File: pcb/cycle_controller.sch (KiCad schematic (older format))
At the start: 51 parts

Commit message: BOM, fixes
Finished assigning parts, footprints except generic resistors
Added series resistors for logic signals received by UI computer to protect against UI computer power-down
Added tolerance notes on main schem
Replaced PSol fuse with PTC
Enlarged PSol driver bypass resistors to 0 ohm
Changed PSol unpopulated current-limiting resistor to divider
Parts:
- C? (x9): Dielectric (none) -> X7R; Manufacturer (none) -> Kemet; Manufacturer PN (none) -> C0603C104K5RACTU; Voltage (none) -> 50V
- C? (x3): Dielectric (none) -> X7R; Manufacturer (none) -> Kemet; Manufacturer PN (none) -> C0805C105K5RACTU; Voltage (none) -> 50V
- C? (x2): Manufacturer (none) -> Kemet; Manufacturer PN (none) -> C0603C180J5GACTU; Voltage (none) -> 50V
- C? (x2): Dielectric (none) -> NP0; Manufacturer (none) -> Kemet; Manufacturer PN (none) -> C0603C689J5GACTU; Voltage (none) -> 50V
- J?: Manufacturer (none) -> Sullins; Manufacturer PN (none) -> PPPC061LFBN-RC
- J? (x2): Manufacturer (none) -> Sullins; Manufacturer PN (none) -> PPPC081LFBN-RC
- J?: Manufacturer (none) -> Sullins; Manufacturer PN (none) -> PPPC101LFBN-RC
- J?: Manufacturer (none) -> Molex; Manufacturer PN (none) -> 503182-1852
- J? (x2): Manufacturer (none) -> Molex; Manufacturer PN (none) -> 43650-0315
- SW? (x2): footprint RespiraWorks_Std:SW_Push_6x6_TD-0341 -> RespiraWorks_Std:SW_Push_6x6; Manufacturer (none) -> C&K; Manufacturer PN (none) -> PTS645SK50SMTR92 LFS
- U?: Manufacturer (none) -> STMicroelectronics; Manufacturer PN (none) -> STM32L496VGT6; Sourcing Notes (none) -> Either ...VGT6 or ...VGT3 can be used
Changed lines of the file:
@@
 F 2 "RespiraWorks_Std:C_0603_1608Metric" H 7538 850 50  0001 C CNN
 F 3 "~" H 7500 1000 50  0001 C CNN
+F 4 "X7R" H 7500 1000 50  0001 C CNN "Dielectric"
+F 5 "Kemet" H 7500 1000 50  0001 C CNN "Manufacturer"
+F 6 "C0603C104K5RACTU" H 7500 1000 50  0001 C CNN "Manufacturer PN"
+F 7 "50V" H 7500 1000 50  0001 C CNN "Voltage"
 	1    7500 1000
 	1    0    0    -1
@@
 F 2 "RespiraWorks_Std:C_0603_1608Metric" H 7838 850 50  0001 C CNN
 F 3 "~" H 7800 1000 50  0001 C CNN
+F 4 "X7R" H 7800 1000 50  0001 C CNN "Dielectric"
+F 5 "Kemet" H 7800 1000 50  0001 C CNN "Manufacturer"
+F 6 "C0603C104K5RACTU" H 7800 1000 50  0001 C CNN "Manufacturer PN"
+F 7 "50V" H 7800 1000 50  0001 C CNN "Voltage"
 	1    7800 1000
 	1    0    0    -1
@@
 F 2 "RespiraWorks_Std:C_0603_1608Metric" H 8188 850 50  0001 C CNN
 F 3 "~" H 8150 1000 50  0001 C CNN
+F 4 "X7R" H 8150 1000 50  0001 C CNN "Dielectric"
+F 5 "Kemet" H 8150 1000 50  0001 C CNN "Manufacturer"
+F 6 "C0603C104K5RACTU" H 8150 1000 50  0001 C CNN "Manufacturer PN"
+F 7 "50V" H 8150 1000 50  0001 C CNN "Voltage"
 	1    8150 1000
 	1    0    0    -1
@@
 F 2 "RespiraWorks_Std:C_0603_1608Metric" H 8488 850 50  0001 C CNN
 F 3 "~" H 8450 1000 50  0001 C CNN
+F 4 "X7R" H 8450 1000 50  0001 C CNN "Dielectric"
+F 5 "Kemet" H 8450 1000 50  0001 C CNN "Manufacturer"
+F 6 "C0603C104K5RACTU" H 8450 1000 50  0001 C CNN "Manufacturer PN"
+F 7 "50V" H 8450 1000 50  0001 C CNN "Voltage"
 	1    8450 1000
 	1    0    0    -1
@@
 F 2 "RespiraWorks_Std:C_0603_1608Metric" H 9588 900 50  0001 C CNN
 F 3 "~" H 9550 1050 50  0001 C CNN
+F 4 "X7R" H 9550 1050 50  0001 C CNN "Dielectric"
+F 5 "Kemet" H 9550 1050 50  0001 C CNN "Manufacturer"
+F 6 "C0603C104K5RACTU" H 9550 1050 50  0001 C CNN "Manufacturer PN"
+F 7 "50V" H 9550 1050 50  0001 C CNN "Voltage"
 	1    9550 1050
 	1    0    0    -1
@@
 F 2 "RespiraWorks_Std:C_0603_1608Metric" H 9938 900 50  0001 C CNN
 F 3 "~" H 9900 1050 50  0001 C CNN
+F 4 "X7R" H 9900 1050 50  0001 C CNN "Dielectric"
+F 5 "Kemet" H 9900 1050 50  0001 C CNN "Manufacturer"
+F 6 "C0805C105K5RACTU" H 9900 1050 50  0001 C CNN "Manufacturer PN"
+F 7 "50V" H 9900 1050 50  0001 C CNN "Voltage"
 	1    9900 1050
 	1    0    0    -1
@@
 F 2 "RespiraWorks_Std:C_0603_1608Metric" H 4738 1600 50  0001 C CNN
 F 3 "~" H 4700 1750 50  0001 C CNN
+F 4 "X7R" H 4700 1750 50  0001 C CNN "Dielectric"
+F 5 "Kemet" H 4700 1750 50  0001 C CNN "Manufacturer"
+F 6 "C0603C104K5RACTU" H 4700 1750 50  0001 C CNN "Manufacturer PN"
+F 7 "50V" H 4700 1750 50  0001 C CNN "Voltage"
 	1    4700 1750
 	1    0    0    -1
@@
 F 0 "SW?" V 4054 1948 50  0000 L CNN
 F 1 "Reset CC" V 4145 1948 50  0000 L CNN
-F 2 "RespiraWorks_Std:SW_Push_6x6_TD-0341" H 4100 2000 50  0001 C CNN
+F 2 "RespiraWorks_Std:SW_Push_6x6" H 4100 2000 50  0001 C CNN
 F 3 "" H 4100 2000 50  0001 C CNN
+F 4 "C&K" H 4100 1800 50  0001 C CNN "Manufacturer"
+F 5 "PTS645SK50SMTR92 LFS" H 4100 1800 50  0001 C CNN "Manufacturer PN"
 	1    4100 1800
 	0    1    1    0
@@
 F 4 "DNP" V 2600 2500 50  0000 L CNN "DNP"
 F 5 "NP0" H 2550 2700 50  0001 C CNN "Dielectric"
+F 6 "Kemet" H 2550 2700 50  0001 C CNN "Manufacturer"
+F 7 "C0603C180J5GACTU" H 2550 2700 50  0001 C CNN "Manufacturer PN"
+F 8 "50V" H 2550 2700 50  0001 C CNN "Voltage"
 	1    2550 2700
 	0    -1   -1   0
@@
 F 4 "DNP" V 2600 3050 50  0000 L CNN "DNP"
 F 5 "NP0" H 2550 3250 50  0001 C CNN "Dielectric"
+F 6 "Kemet" H 2550 3250 50  0001 C CNN "Manufacturer"
+F 7 "C0603C180J5GACTU" H 2550 3250 50  0001 C CNN "Manufacturer PN"
+F 8 "50V" H 2550 3250 50  0001 C CNN "Voltage"
 	1    2550 3250
 	0    -1   -1   0
@@
 F 3 "~" H 3600 5050 50  0001 C CNN
 F 4 "" V 3950 5050 50  0001 C CNN "DNP"
+F 5 "NP0" H 3600 5050 50  0001 C CNN "Dielectric"
+F 6 "Kemet" H 3600 5050 50  0001 C CNN "Manufacturer"
+F 7 "C0603C689J5GACTU" H 3600 5050 50  0001 C CNN "Manufacturer PN"
+F 8 "50V" H 3600 5050 50  0001 C CNN "Voltage"
 	1    3600 5050
 	0    1    1    0
@@
 F 0 "SW?" V 2154 4698 50  0000 L CNN
 F 1 "User TBD" V 2245 4698 50  0000 L CNN
-F 2 "RespiraWorks_Std:SW_Push_6x6_TD-0341" H 2200 4750 50  0001 C CNN
+F 2 "RespiraWorks_Std:SW_Push_6x6" H 2200 4750 50  0001 C CNN
 F 3 "" H 2200 4750 50  0001 C CNN
+F 4 "C&K" H 2200 4550 50  0001 C CNN "Manufacturer"
+F 5 "PTS645SK50SMTR92 LFS" H 2200 4550 50  0001 C CNN "Manufacturer PN"
 	1    2200 4550
 	0    1    1    0
@@
 F 2 "RespiraWorks_Std:C_0603_1608Metric" H 1638 4350 50  0001 C CNN
 F 3 "~" H 1600 4500 50  0001 C CNN
+F 4 "X7R" H 1600 4500 50  0001 C CNN "Dielectric"
+F 5 "Kemet" H 1600 4500 50  0001 C CNN "Manufacturer"
+F 6 "C0603C104K5RACTU" H 1600 4500 50  0001 C CNN "Manufacturer PN"
+F 7 "50V" H 1600 4500 50  0001 C CNN "Voltage"
 	1    1600 4500
 	1    0    0    -1
@@
 F 2 "RespiraWorks:SD_Molex_5031821852" H 3050 6250 50  0001 C CNN
 F 3 "https://www.molex.com/pdm_docs/sd/5031821852_sd.pdf" H 3650 6150 50  0001 C CNN
+F 4 "Molex" H 2250 6650 50  0001 C CNN "Manufacturer"
+F 5 "503182-1852" H 2250 6650 50  0001 C CNN "Manufacturer PN"
 	1    2250 6650
 	1    0    0    -1
@@
 F 2 "RespiraWorks_Std:C_0603_1608Metric" H 2938 6150 50  0001 C CNN
 F 3 "~" H 2900 6300 50  0001 C CNN
+F 4 "X7R" H 2900 6300 50  0001 C CNN "Dielectric"
+F 5 "Kemet" H 2900 6300 50  0001 C CNN "Manufacturer"
+F 6 "C0805C105K5RACTU" H 2900 6300 50  0001 C CNN "Manufacturer PN"
+F 7 "50V" H 2900 6300 50  0001 C CNN "Voltage"
 	1    2900 6300
 	1    0    0    -1
@@
 F 2 "RespiraWorks_Std:C_0603_1608Metric" H 3338 6150 50  0001 C CNN
 F 3 "~" H 3300 6300 50  0001 C CNN
+F 4 "X7R" H 3300 6300 50  0001 C CNN "Dielectric"
+F 5 "Kemet" H 3300 6300 50  0001 C CNN "Manufacturer"
+F 6 "C0603C104K5RACTU" H 3300 6300 50  0001 C CNN "Manufacturer PN"
+F 7 "50V" H 3300 6300 50  0001 C CNN "Voltage"
 	1    3300 6300
 	1    0    0    -1
@@
 F 2 "RespiraWorks_Std:PinSocket_1x06_P2.54mm_Vertical" H 10700 3400 50  0001 C CNN
 F 3 "~" H 10700 3400 50  0001 C CNN
+F 4 "Sullins" H 10700 3400 50  0001 C CNN "Manufacturer"
+F 5 "PPPC061LFBN-RC" H 10700 3400 50  0001 C CNN "Manufacturer PN"
 	1    10700 3400
 	1    0    0    -1
@@
 F 2 "RespiraWorks_Std:PinSocket_1x08_P2.54mm_Vertical" H 10700 5850 50  0001 C CNN
 F 3 "~" H 10700 5850 50  0001 C CNN
+F 4 "Sullins" H 10700 5850 50  0001 C CNN "Manufacturer"
+F 5 "PPPC081LFBN-RC" H 10700 5850 50  0001 C CNN "Manufacturer PN"
 	1    10700 5850
 	1    0    0    -1
@@
 F 2 "RespiraWorks_Std:PinSocket_1x10_P2.54mm_Vertical" H 10700 4700 50  0001 C CNN
 F 3 "~" H 10700 4700 50  0001 C CNN
+F 4 "Sullins" H 10700 4700 50  0001 C CNN "Manufacturer"
+F 5 "PPPC101LFBN-RC" H 10700 4700 50  0001 C CNN "Manufacturer PN"
 	1    10700 4700
 	1    0    0    -1
@@
 F 2 "RespiraWorks_Std:PinSocket_1x08_P2.54mm_Vertical" H 10700 2550 50  0001 C CNN
 F 3 "~" H 10700 2550 50  0001 C CNN
+F 4 "Sullins" H 10700 2550 50  0001 C CNN "Manufacturer"
+F 5 "PPPC081LFBN-RC" H 10700 2550 50  0001 C CNN "Manufacturer PN"
 	1    10700 2550
 	1    0    0    -1
@@
 F 2 "RespiraWorks_Std:C_0603_1608Metric" H 4638 950 50  0001 C CNN
 F 3 "~" H 4600 1100 50  0001 C CNN
+F 4 "X7R" H 4600 1100 50  0001 C CNN "Dielectric"
+F 5 "Kemet" H 4600 1100 50  0001 C CNN "Manufacturer"
+F 6 "C0805C105K5RACTU" H 4600 1100 50  0001 C CNN "Manufacturer PN"
+F 7 "50V" H 4600 1100 50  0001 C CNN "Voltage"
 	1    4600 1100
 	1    0    0    -1
@@
 F 3 "~" H 3600 4600 50  0001 C CNN
 F 4 "" V 3450 4400 50  0001 C CNN "DNP"
+F 5 "NP0" H 3600 4600 50  0001 C CNN "Dielectric"
+F 6 "Kemet" H 3600 4600 50  0001 C CNN "Manufacturer"
+F 7 "C0603C689J5GACTU" H 3600 4600 50  0001 C CNN "Manufacturer PN"
+F 8 "50V" H 3600 4600 50  0001 C CNN "Voltage"
 	1    3600 4600
 	0    1    1    0
@@
 F 2 "RespiraWorks_Std:Molex_Micro-Fit_3.0_43650-0315_1x03_P3.00mm_Vertical" H 1100 1000 50  0001 C CNN
 F 3 "~" H 1100 1000 50  0001 C CNN
+F 4 "Molex" H 1100 1000 50  0001 C CNN "Manufacturer"
+F 5 "43650-0315" H 1100 1000 50  0001 C CNN "Manufacturer PN"
 	1    1100 1000
 	-1   0    0    -1
@@
 F 2 "RespiraWorks_Std:Molex_Micro-Fit_3.0_43650-0315_1x03_P3.00mm_Vertical" H 1100 1600 50  0001 C CNN
 F 3 "~" H 1100 1600 50  0001 C CNN
+F 4 "Molex" H 1100 1600 50  0001 C CNN "Manufacturer"
+F 5 "43650-0315" H 1100 1600 50  0001 C CNN "Manufacturer PN"
 	1    1100 1600
 	-1   0    0    -1
@@
 F 2 "RespiraWorks_Std:LQFP-100_14x14mm_P0.5mm" H 6550 -900 50  0001 R CNN
 F 3 "http://www.st.com/st-web-https://www.st.com/resource/en/datasheet/stm32l496vg.pdf" H 5800 3200 50  0001 C CNN
+F 4 "STMicroelectronics" H 5800 3200 50  0001 C CNN "Manufacturer"
+F 5 "STM32L496VGT6" H 5800 3200 50  0001 C CNN "Manufacturer PN"
+F 6 "Either ...VGT6 or ...VGT3 can be used" H 5800 3200 50  0001 C CNN "Sourcing Notes"
 	1    5800 3200
 	1    0    0    -1
@@
 F 2 "RespiraWorks_Std:C_0603_1608Metric" H 4638 2150 50  0001 C CNN
 F 3 "~" H 4600 2300 50  0001 C CNN
+F 4 "X7R" H 4600 2300 50  0001 C CNN "Dielectric"
+F 5 "Kemet" H 4600 2300 50  0001 C CNN "Manufacturer"
+F 6 "C0603C104K5RACTU" H 4600 2300 50  0001 C CNN "Manufacturer PN"
+F 7 "50V" H 4600 2300 50  0001 C CNN "Voltage"
 	1    4600 2300
 	1    0    0    -1

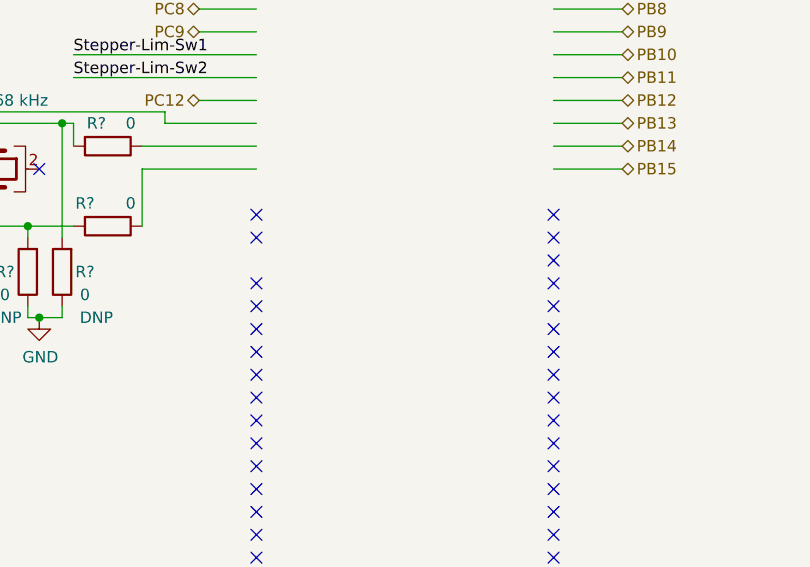
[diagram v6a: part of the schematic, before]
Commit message: New stepper driver, CC testpoints
Switched stepper driver to L6470 for availability
Added testpoints to unused GPIO pins on cycle controller for debug/rework
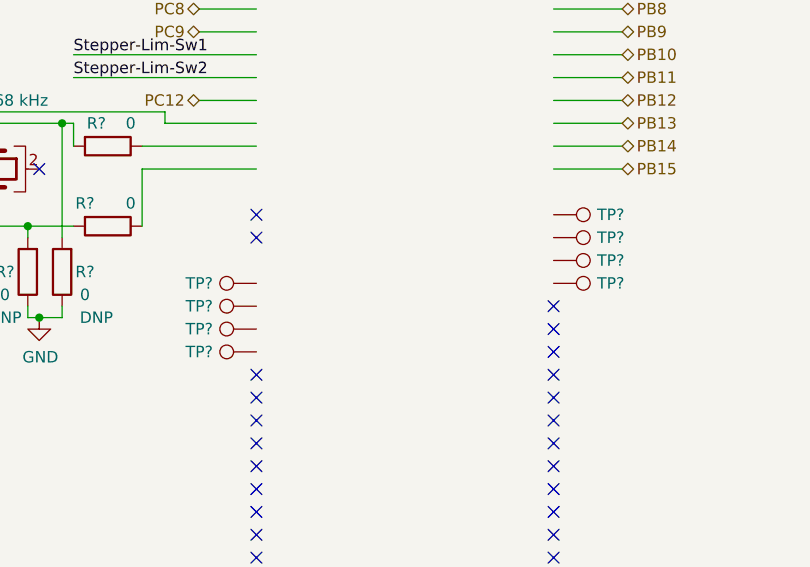
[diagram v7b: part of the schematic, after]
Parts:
- added TP?: PE0, RespiraWorks_Std:TestPoint_Pad_2.0x2.0mm, symbol Connector:TestPoint
- added TP?: PE1, RespiraWorks_Std:TestPoint_Pad_2.0x2.0mm, symbol Connector:TestPoint
- added TP?: PE2, RespiraWorks_Std:TestPoint_Pad_2.0x2.0mm, symbol Connector:TestPoint
- added TP?: PE3, RespiraWorks_Std:TestPoint_Pad_2.0x2.0mm, symbol Connector:TestPoint
- added TP?: PD3, RespiraWorks_Std:TestPoint_Pad_2.0x2.0mm, symbol Connector:TestPoint
- added TP?: PD4, RespiraWorks_Std:TestPoint_Pad_2.0x2.0mm, symbol Connector:TestPoint
- added TP?: PD5, RespiraWorks_Std:TestPoint_Pad_2.0x2.0mm, symbol Connector:TestPoint
- added TP?: PD6, RespiraWorks_Std:TestPoint_Pad_2.0x2.0mm, symbol Connector:TestPoint
- TP?: value TP -> SPI-MISO
- TP?: value TP -> SPI-MOSI
- TP?: value TP -> SPI-SCLK
- TP?: value TP -> uSD-nCS
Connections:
- no-connect marks 38 -> 30
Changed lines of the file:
@@
 AR Path="/5FCD4D18/60D43B3D" Ref="TP?"  Part="1"
 F 0 "TP?" H 4250 7450 50  0000 C CNN
-F 1 "TP" V 4300 7300 50  0001 C CNN
+F 1 "SPI-MISO" V 4300 7300 50  0001 C CNN
 F 2 "RespiraWorks_Std:TestPoint_Pad_2.0x2.0mm" H 4450 7250 50  0001 C CNN
 F 3 "~" H 4450 7250 50  0001 C CNN
@@
 AR Path="/5FCD4D18/60D53337" Ref="TP?"  Part="1"
 F 0 "TP?" H 4450 7450 50  0000 C CNN
-F 1 "TP" V 4500 7300 50  0001 C CNN
+F 1 "SPI-MOSI" V 4500 7300 50  0001 C CNN
 F 2 "RespiraWorks_Std:TestPoint_Pad_2.0x2.0mm" H 4650 7250 50  0001 C CNN
 F 3 "~" H 4650 7250 50  0001 C CNN
@@
 AR Path="/5FCD4D18/60D53971" Ref="TP?"  Part="1"
 F 0 "TP?" H 4650 7450 50  0000 C CNN
-F 1 "TP" V 4700 7300 50  0001 C CNN
+F 1 "SPI-SCLK" V 4700 7300 50  0001 C CNN
 F 2 "RespiraWorks_Std:TestPoint_Pad_2.0x2.0mm" H 4850 7250 50  0001 C CNN
 F 3 "~" H 4850 7250 50  0001 C CNN
@@
 AR Path="/5FCD4D18/60D5400C" Ref="TP?"  Part="1"
 F 0 "TP?" H 4850 7450 50  0000 C CNN
-F 1 "TP" V 4900 7300 50  0001 C CNN
+F 1 "uSD-nCS" V 4900 7300 50  0001 C CNN
 F 2 "RespiraWorks_Std:TestPoint_Pad_2.0x2.0mm" H 5050 7250 50  0001 C CNN
 F 3 "~" H 5050 7250 50  0001 C CNN
@@
 Wire Wire Line
 	3100 6100 3300 6100
-$Comp
-L RespiraWorks:STM32L496VGT U?
-U 1 1 60565F40
-P 5800 3200
-F 0 "U?" H 5800 -1100 50  0000 C CNN
-F 1 "STM32L496VGT" H 5800 -1200 50  0000 C CNN
-F 2 "RespiraWorks_Std:LQFP-100_14x14mm_P0.5mm" H 6550 -900 50  0001 R CNN
-F 3 "http://www.st.com/st-web-https://www.st.com/resource/en/datasheet/stm32l496vg.pdf" H 5800 3200 50  0001 C CNN
-F 4 "STMicroelectronics" H 5800 3200 50  0001 C CNN "Manufacturer"
-F 5 "STM32L496VGT6" H 5800 3200 50  0001 C CNN "Manufacturer PN"
-F 6 "Either ...VGT6 or ...VGT3 can be used" H 5800 3200 50  0001 C CNN "Sourcing Notes"
-	1    5800 3200
-	1    0    0    -1
-$EndComp
 Wire Wire Line
 	6000 750  5900 750
@@
 	5500 7200 5600 7200
 Connection ~ 5600 7200
-NoConn ~ 6400 5000
-NoConn ~ 6400 5100
-NoConn ~ 6400 5200
-NoConn ~ 6400 5300
 NoConn ~ 6400 5400
 NoConn ~ 6400 5500
@@
 NoConn ~ 5100 5800
 NoConn ~ 5100 5700
-NoConn ~ 5100 5600
-NoConn ~ 5100 5500
-NoConn ~ 5100 5400
-NoConn ~ 5100 5300
 NoConn ~ 5100 5100
 NoConn ~ 5100 5000
+$Comp
+L Connector:TestPoint TP?
+U 1 1 6098EDD0
+P 6400 5000
+AR Path="/5FCD50A5/6098EDD0" Ref="TP?"  Part="1"
+AR Path="/6052CC9F/6098EDD0" Ref="TP?"  Part="1"
+AR Path="/6098EDD0" Ref="TP?"  Part="1"
+AR Path="/5FCD4D18/6098EDD0" Ref="TP?"  Part="1"
+F 0 "TP?" V 6400 5250 50  0000 C CNN
+F 1 "PE0" V 6450 5050 50  0001 C CNN
+F 2 "RespiraWorks_Std:TestPoint_Pad_2.0x2.0mm" H 6600 5000 50  0001 C CNN
+F 3 "~" H 6600 5000 50  0001 C CNN
+	1    6400 5000
+	0    1    1    0
+$EndComp
+$Comp
+L Connector:TestPoint TP?
+U 1 1 60993E18
+P 6400 5100
+AR Path="/5FCD50A5/60993E18" Ref="TP?"  Part="1"
+AR Path="/6052CC9F/60993E18" Ref="TP?"  Part="1"
+AR Path="/60993E18" Ref="TP?"  Part="1"
+AR Path="/5FCD4D18/60993E18" Ref="TP?"  Part="1"
+F 0 "TP?" V 6400 5350 50  0000 C CNN
+F 1 "PE1" V 6450 5150 50  0001 C CNN
+F 2 "RespiraWorks_Std:TestPoint_Pad_2.0x2.0mm" H 6600 5100 50  0001 C CNN
+F 3 "~" H 6600 5100 50  0001 C CNN
+	1    6400 5100
+	0    1    1    0
+$EndComp
+$Comp
+L Connector:TestPoint TP?
+U 1 1 609942B7
+P 6400 5200
+AR Path="/5FCD50A5/609942B7" Ref="TP?"  Part="1"
+AR Path="/6052CC9F/609942B7" Ref="TP?"  Part="1"
+AR Path="/609942B7" Ref="TP?"  Part="1"
+AR Path="/5FCD4D18/609942B7" Ref="TP?"  Part="1"
+F 0 "TP?" V 6400 5450 50  0000 C CNN
+F 1 "PE2" V 6450 5250 50  0001 C CNN
+F 2 "RespiraWorks_Std:TestPoint_Pad_2.0x2.0mm" H 6600 5200 50  0001 C CNN
+F 3 "~" H 6600 5200 50  0001 C CNN
+	1    6400 5200
+	0    1    1    0
+$EndComp
+$Comp
+L Connector:TestPoint TP?
+U 1 1 6099470B
+P 6400 5300
+AR Path="/5FCD50A5/6099470B" Ref="TP?"  Part="1"
+AR Path="/6052CC9F/6099470B" Ref="TP?"  Part="1"
+AR Path="/6099470B" Ref="TP?"  Part="1"
+AR Path="/5FCD4D18/6099470B" Ref="TP?"  Part="1"
+F 0 "TP?" V 6400 5550 50  0000 C CNN
+F 1 "PE3" V 6450 5350 50  0001 C CNN
+F 2 "RespiraWorks_Std:TestPoint_Pad_2.0x2.0mm" H 6600 5300 50  0001 C CNN
+F 3 "~" H 6600 5300 50  0001 C CNN
+	1    6400 5300
+	0    1    1    0
+$EndComp
+$Comp
+L RespiraWorks:STM32L496VGT U?
+U 1 1 60565F40
+P 5800 3200
+F 0 "U?" H 5800 -1100 50  0000 C CNN
+F 1 "STM32L496VGT" H 5800 -1200 50  0000 C CNN
+F 2 "RespiraWorks_Std:LQFP-100_14x14mm_P0.5mm" H 6550 -900 50  0001 R CNN
+F 3 "http://www.st.com/st-web-https://www.st.com/resource/en/datasheet/stm32l496vg.pdf" H 5800 3200 50  0001 C CNN
+F 4 "STMicroelectronics" H 5800 3200 50  0001 C CNN "Manufacturer"
+F 5 "STM32L496VGT6" H 5800 3200 50  0001 C CNN "Manufacturer PN"
+F 6 "Either ...VGT6 or ...VGT3 can be used" H 5800 3200 50  0001 C CNN "Sourcing Notes"
+	1    5800 3200
+	1    0    0    -1
+$EndComp
+$Comp
+L Connector:TestPoint TP?
+U 1 1 60995F5D
+P 5100 5300
+AR Path="/5FCD50A5/60995F5D" Ref="TP?"  Part="1"
+AR Path="/6052CC9F/60995F5D" Ref="TP?"  Part="1"
+AR Path="/60995F5D" Ref="TP?"  Part="1"
+AR Path="/5FCD4D18/60995F5D" Ref="TP?"  Part="1"
+F 0 "TP?" V 5100 5550 50  0000 C CNN
+F 1 "PD3" V 5150 5350 50  0001 C CNN
+F 2 "RespiraWorks_Std:TestPoint_Pad_2.0x2.0mm" H 5300 5300 50  0001 C CNN
+F 3 "~" H 5300 5300 50  0001 C CNN
+	1    5100 5300
+	0    -1   -1   0
+$EndComp
+$Comp
+L Connector:TestPoint TP?
+U 1 1 60996952
+P 5100 5400
+AR Path="/5FCD50A5/60996952" Ref="TP?"  Part="1"
+AR Path="/6052CC9F/60996952" Ref="TP?"  Part="1"
+AR Path="/60996952" Ref="TP?"  Part="1"
+AR Path="/5FCD4D18/60996952" Ref="TP?"  Part="1"
+F 0 "TP?" V 5100 5650 50  0000 C CNN
+F 1 "PD4" V 5150 5450 50  0001 C CNN
+F 2 "RespiraWorks_Std:TestPoint_Pad_2.0x2.0mm" H 5300 5400 50  0001 C CNN
+F 3 "~" H 5300 5400 50  0001 C CNN
+	1    5100 5400
+	0    -1   -1   0
+$EndComp
+$Comp
+L Connector:TestPoint TP?
+U 1 1 60996E2E
+P 5100 5500
+AR Path="/5FCD50A5/60996E2E" Ref="TP?"  Part="1"
+AR Path="/6052CC9F/60996E2E" Ref="TP?"  Part="1"
+AR Path="/60996E2E" Ref="TP?"  Part="1"
+AR Path="/5FCD4D18/60996E2E" Ref="TP?"  Part="1"
+F 0 "TP?" V 5100 5750 50  0000 C CNN
+F 1 "PD5" V 5150 5550 50  0001 C CNN
+F 2 "RespiraWorks_Std:TestPoint_Pad_2.0x2.0mm" H 5300 5500 50  0001 C CNN
+F 3 "~" H 5300 5500 50  0001 C CNN
+	1    5100 5500
+	0    -1   -1   0
+$EndComp
+$Comp
+L Connector:TestPoint TP?
+U 1 1 60997344
+P 5100 5600
+AR Path="/5FCD50A5/60997344" Ref="TP?"  Part="1"
+AR Path="/6052CC9F/60997344" Ref="TP?"  Part="1"
+AR Path="/60997344" Ref="TP?"  Part="1"
+AR Path="/5FCD4D18/60997344" Ref="TP?"  Part="1"
+F 0 "TP?" V 5100 5850 50  0000 C CNN
+F 1 "PD6" V 5150 5650 50  0001 C CNN
+F 2 "RespiraWorks_Std:TestPoint_Pad_2.0x2.0mm" H 5300 5600 50  0001 C CNN
+F 3 "~" H 5300 5600 50  0001 C CNN
+	1    5100 5600
+	0    -1   -1   0
+$EndComp
 $EndSCHEMATC

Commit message: Symbols
Re-assigned transistor symbols to Device:* and RespiraWorks_Std:*
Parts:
- SW? (x2): symbol Switch:SW_Push -> RespiraWorks_Std:SW_Push
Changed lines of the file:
@@
 $EndComp
 $Comp
-L Switch:SW_Push SW?
+L RespiraWorks_Std:SW_Push SW?
 U 1 1 5FED4D7F
 P 4100 1800
@@
 	6400 3700 6700 3700
 $Comp
-L Switch:SW_Push SW?
+L RespiraWorks_Std:SW_Push SW?
 U 1 1 5FF60966
 P 2200 4550
